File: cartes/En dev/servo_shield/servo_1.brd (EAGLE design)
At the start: 55.8 x 54.8 mm, 33 parts, among them X1 5V_INPUT, X2 12V_INPUT

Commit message: Fix du bug #5 avec l'ajout d'un treansceiver RS485 pour l'ax12
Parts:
- removed JP6: RX_TX_Connxion, SparkFun-Passives:1X02
- added U1: SN65HVD08D, Texas Instruments_By_element14_Batch_1:SOIC127P600X175-8N
- moved LED_12V 25.4 mm to (38.5, 25.3), turned to 270 degrees
- moved LED_5V 24.7 mm to (27.0, 47.9), turned to 90 degrees
- moved PUISSANCE 3.14 mm to (53.6, 25.2)
- moved R3 1.31 mm to (35.8, 27.0)
- moved ADUM1250 1.18 mm to (40.9, 30.0)
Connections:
- net RXTX_OUT renamed RXTX_DIRTY
- new net RXTX: ADUM1250.3, U1.6
- net GND: now also U1.5
- net N$4: now also LED_12V.A; no longer LED_5V.A
- net N$6: now also LED_5V.A; no longer LED_12V.A
- net OUT4: now also U1.2, U1.3
- net RXI: now also U1.1; no longer JP6.2
- net TXO: now also U1.4; no longer ADUM1250.3, JP6.1
- net VCC: now also U1.8
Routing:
- net RXI: track 3.09 -> 52.8 mm
- net OUT4: track 7.81 -> 27.1 mm, vias 0 -> 1
- net OUT8: track 33.6 -> 21.4 mm, vias 1 -> 0
- net PWM9: track 15.1 -> 25.8 mm, vias 0 -> 1
- net GND: track 5.22 -> 12.1 mm, vias 2 -> 3
- net RXTX: track 0.00 -> 3.66 mm, vias 0 -> 1
- net 5V_DIRTY: track 94.3 -> 90.8 mm
- net PWM9_OUT: track 11.5 -> 14.8 mm
- net TXO: track 49.4 -> 52.7 mm
- net 12V_DIRTY: track 61.4 -> 58.9 mm
- net PWM6: track 25.7 -> 28.0 mm
- net GND_DIRTY: track 18.7 -> 20.5 mm, vias 1 -> 2
- net OUT7: track 22.2 -> 23.9 mm
- net PWM7_OUT: track 4.82 -> 5.93 mm
- net PWM6_OUT: track 8.53 -> 9.46 mm
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
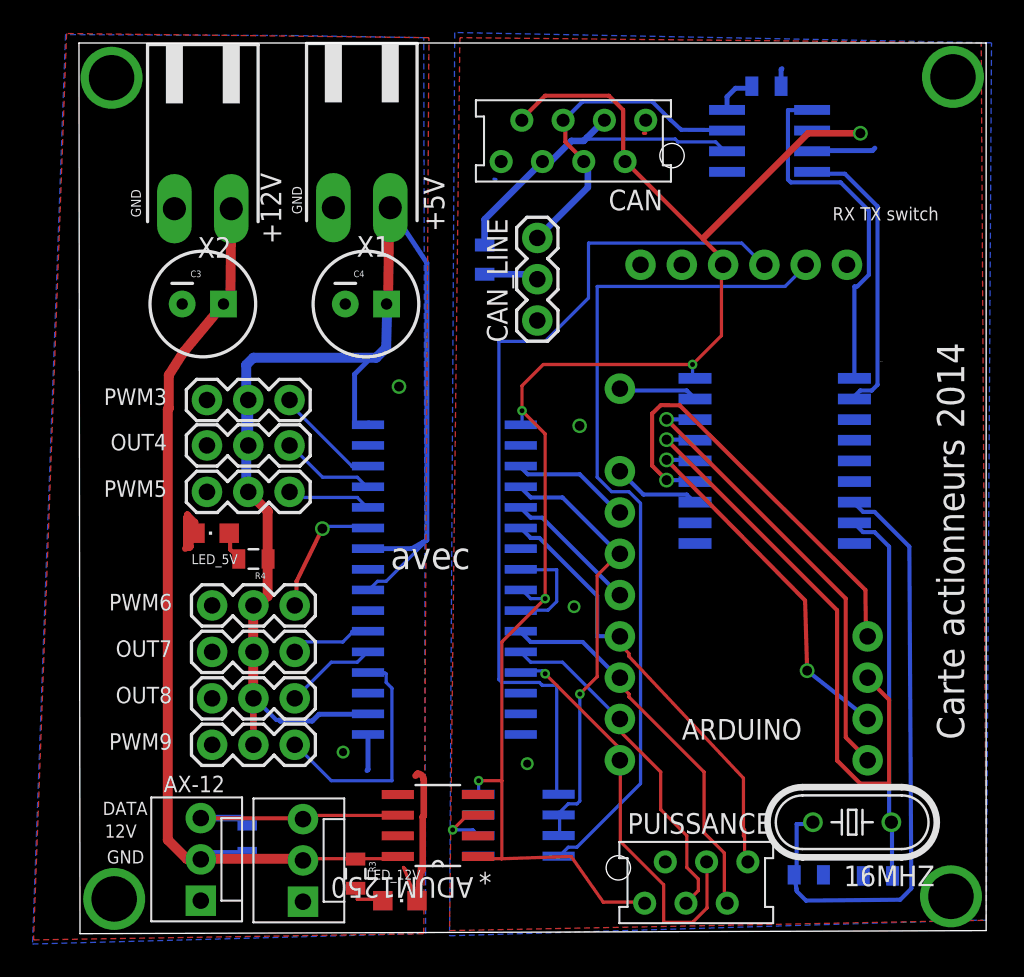
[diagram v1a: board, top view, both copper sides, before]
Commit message: carte mos pwm modifié
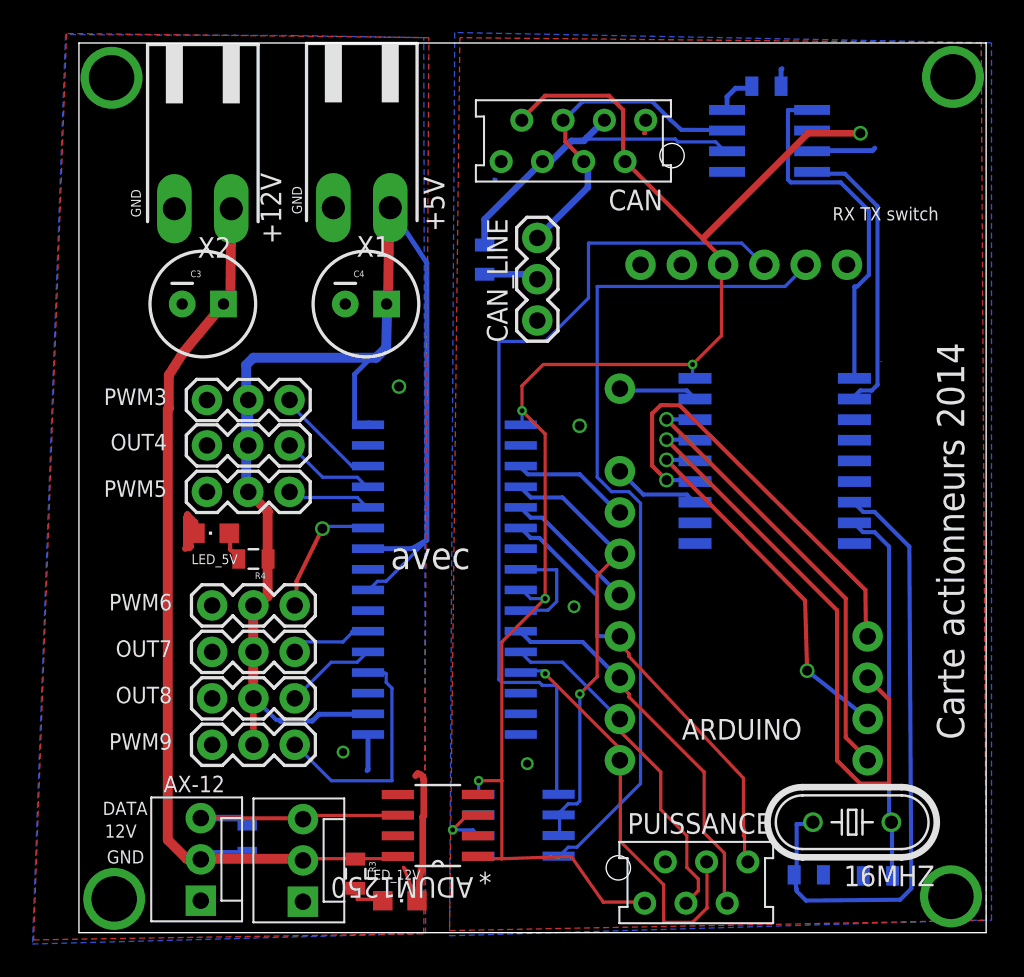
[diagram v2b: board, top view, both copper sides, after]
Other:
- board size 55.8 x 54.8 mm -> 55.8 x 54.7 mm
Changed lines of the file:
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@@
 <?xml version="1.0" encoding="utf-8"?>
 <!DOCTYPE eagle SYSTEM "eagle.dtd">
-<eagle version="6.5.0">
+<eagle version="6.4">
 <drawing>
 <settings>
@@
 <board>
 <plain>
-<wire x1="18.8595" y1="23.3045" x2="74.6" y2="23.495" width="0" layer="20"/>
-<wire x1="74.6" y1="23.495" x2="74.6" y2="78.095" width="0" layer="20"/>
+<wire x1="18.796" y1="23.368" x2="74.6" y2="23.368" width="0" layer="20"/>
+<wire x1="74.6" y1="23.368" x2="74.6" y2="78.095" width="0" layer="20"/>
 <wire x1="74.6" y1="78.095" x2="18.796" y2="78.095" width="0" layer="20"/>
-<wire x1="18.796" y1="78.095" x2="18.8595" y2="23.3045" width="0" layer="20"/>
+<wire x1="18.796" y1="78.095" x2="18.796" y2="23.368" width="0" layer="20"/>
 <polygon width="0.4064" layer="42">
 <vertex x="58.1025" y="57.785"/>
@@
 <vertex x="41.5925" y="23.1775"/>
 <vertex x="73.66" y="24.13"/>
-<vertex x="74.6125" y="24.13"/>
+<vertex x="74.93" y="24.13"/>
 <vertex x="74.93" y="78.105"/>
 <vertex x="41.91" y="78.74"/>

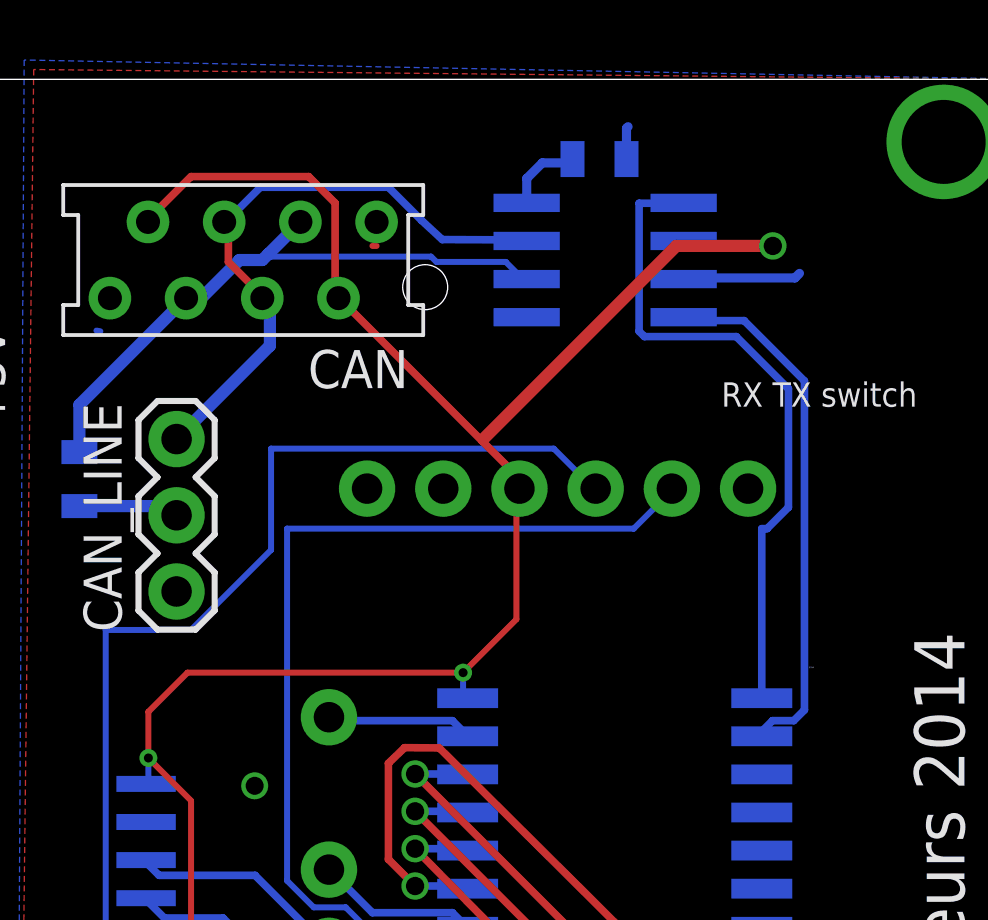
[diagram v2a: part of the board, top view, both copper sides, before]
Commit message: Modif carte sharp et carte servo avec probleme transceiver
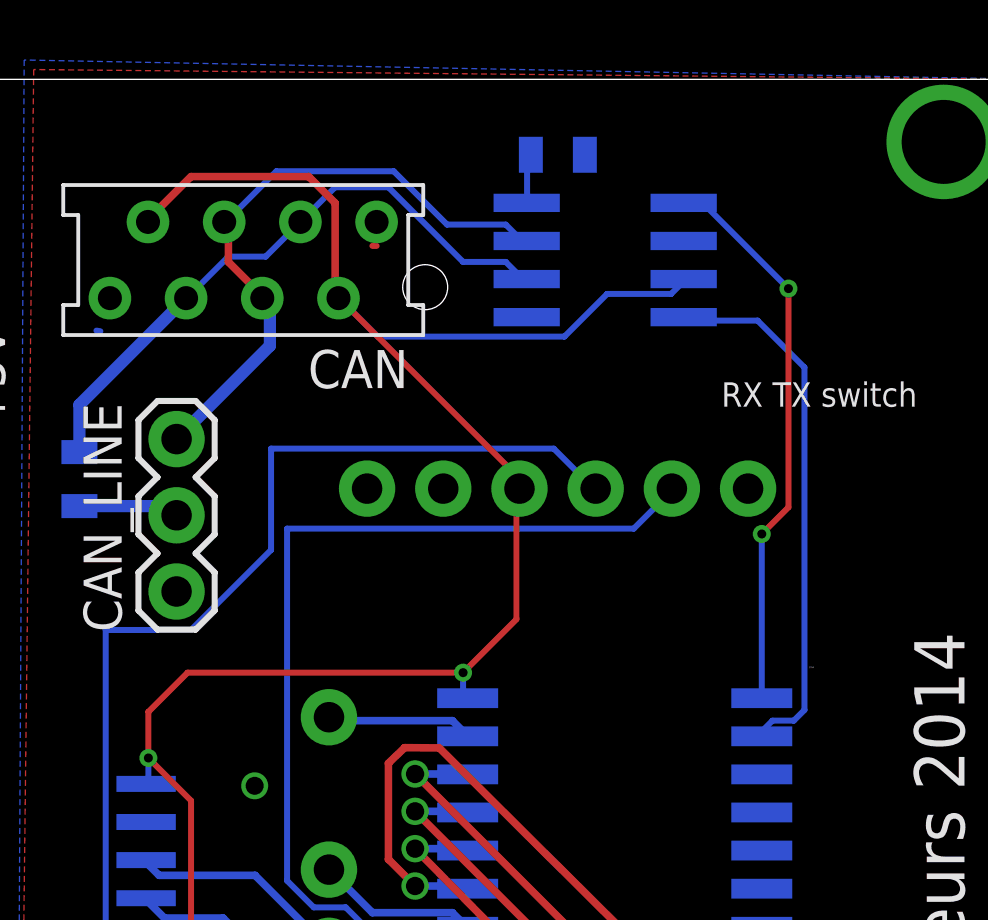
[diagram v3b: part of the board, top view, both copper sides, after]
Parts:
- moved R1 1.39 mm to (59.7, 75.6)
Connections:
- net GND: now also TRANSCEIVER.2; no longer TRANSCEIVER.3
- net VCC: now also TRANSCEIVER.3; no longer TRANSCEIVER.2
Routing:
- net GND: track 12.1 -> 6.88 mm
- net CAN_TXD: track 22.3 -> 18.7 mm, vias 0 -> 2
- net VCC: track 101.2 -> 98.6 mm, vias 5 -> 4
- net N$5: track 2.61 -> 1.72 mm
